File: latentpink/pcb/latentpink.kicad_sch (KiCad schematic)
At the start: 32 parts, among them M10 WEEE, M3 SCREWHOLE, M4 SCREWHOLE, M5 SCREWHOLE, M6 SCREWHOLE, M7 LONGTHING, M8 OSHW, M9 POLARITY, U36 AT30TS74_UDFN, U37 AT30TS74_UDFN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

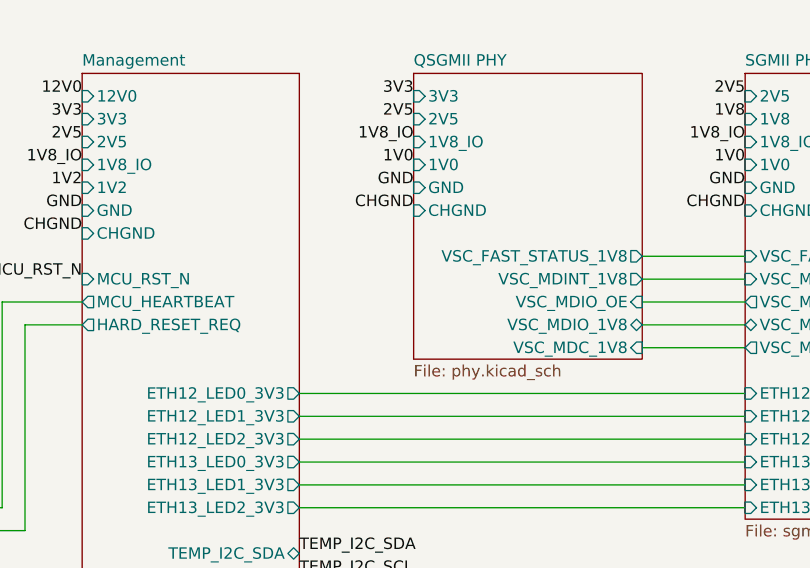
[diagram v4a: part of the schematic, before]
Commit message: Updated PCB layout with changes made during initial FPGA RTL dev
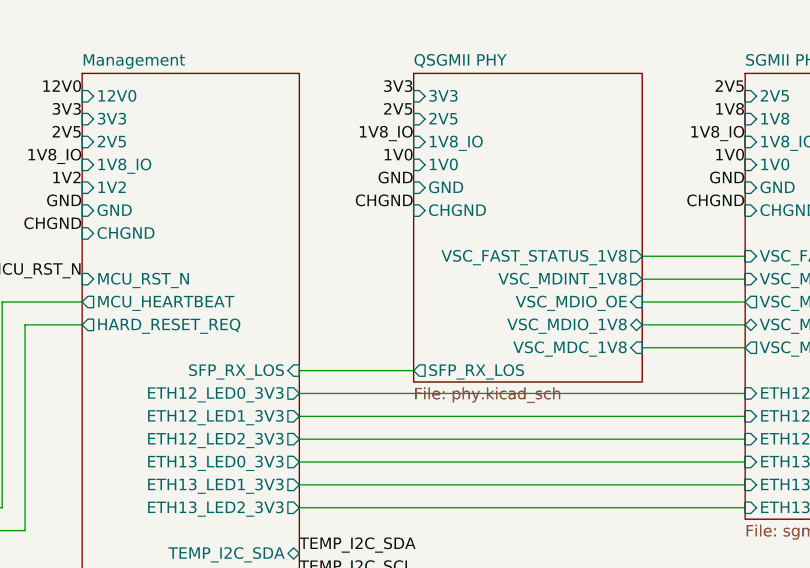
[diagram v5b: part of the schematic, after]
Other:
- sheet Management ports: added SFP_RX_LOS; removed none
- sheet QSGMII PHY ports: added SFP_RX_LOS; removed none
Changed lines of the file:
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@@
   (title_block
     (title "LATENTPINK - Top Level")
-    (date "2023-06-09")
+    (date "2023-06-15")
     (rev "0.1")
     (company "Antikernel Labs")
@@
   )
   (wire (pts (xy 190.5 43.18) (xy 201.93 43.18))
+    (stroke (width 0) (type default) (color 0 0 0 0))
+  )
+  (wire (pts (xy 152.4 55.88) (xy 165.1 55.88))
     (stroke (width 0) (type default) (color 0 0 0 0))
   )
@@
       (effects (font (size 1.27 1.27)) (justify right))
     )
+    (pin "SFP_RX_LOS" input (at 152.4 55.88 0)
+      (effects (font (size 1.27 1.27)) (justify right))
+    )
   )
   (sheet (at 201.93 22.86) (size 22.86 49.53) (fields_autoplaced)
@@
     )
   )
-  (sheet (at 165.1 22.86) (size 25.4 31.75) (fields_autoplaced)
+  (sheet (at 165.1 22.86) (size 25.4 34.29) (fields_autoplaced)
     (stroke (width 0.1524) (type solid) (color 0 0 0 0))
     (fill (color 0 0 0 0.0000))
@@
       (effects (font (size 1.27 1.27)) (justify left bottom))
     )
-    (property "Sheet file" "phy.kicad_sch" (id 1) (at 165.1 55.1946 0)
+    (property "Sheet file" "phy.kicad_sch" (id 1) (at 165.1 57.7346 0)
       (effects (font (size 1.27 1.27)) (justify left top))
     )
@@
     )
     (pin "1V8_IO" input (at 165.1 30.48 180)
+      (effects (font (size 1.27 1.27)) (justify left))
+    )
+    (pin "SFP_RX_LOS" output (at 165.1 55.88 180)
       (effects (font (size 1.27 1.27)) (justify left))
     )
@@
       (reference "C187") (unit 1) (value "0.47 uF") (footprint "azonenberg_pcb:EIA_0402_CAP_NOSILK")
     )
+    (path "/6c4b0638-d970-4292-bc58-db2e1b793524/d5990d76-6ad3-4bfd-a9be-5da547fd1224/96c4edd4-ce50-4a09-a53b-87b5a1a0fc47"
+      (reference "C188") (unit 1) (value "0.47 uF") (footprint "azonenberg_pcb:EIA_0402_CAP_NOSILK")
+    )
     (path "/6c4b0638-d970-4292-bc58-db2e1b793524/d5990d76-6ad3-4bfd-a9be-5da547fd1224/942373ed-08bf-4922-8211-11f3040b6b20"
       (reference "C189") (unit 1) (value "0.47 uF") (footprint "azonenberg_pcb:EIA_0402_CAP_NOSILK")
     )
+    (path "/6c4b0638-d970-4292-bc58-db2e1b793524/d5990d76-6ad3-4bfd-a9be-5da547fd1224/03eef2ac-07fc-4d6a-bbce-01046e92cb60"
+      (reference "C190") (unit 1) (value "0.47 uF") (footprint "azonenberg_pcb:EIA_0402_CAP_NOSILK")
+    )
     (path "/6c4b0638-d970-4292-bc58-db2e1b793524/d5990d76-6ad3-4bfd-a9be-5da547fd1224/da335c01-5e59-445c-8ce9-3cff99fa0a53"
       (reference "C191") (unit 1) (value "0.47 uF") (footprint "azonenberg_pcb:EIA_0402_CAP_NOSILK")
@@
       (reference "C448") (unit 1) (value "0.47 uF") (footprint "azonenberg_pcb:EIA_0402_CAP_NOSILK")
     )
+    (path "/6c4b0638-d970-4292-bc58-db2e1b793524/d5990d76-6ad3-4bfd-a9be-5da547fd1224/b9219748-1c2b-40c0-a041-7b1828d1e843"
+      (reference "C449") (unit 1) (value "0.47 uF") (footprint "azonenberg_pcb:EIA_0402_CAP_NOSILK")
+    )
     (path "/22109ef7-0bd2-46c3-8dd9-ecb52bedcbfa/94c46c58-24dc-4845-8aaa-ab3c82e370b2"
       (reference "C450") (unit 1) (value "0.1 uF") (footprint "azonenberg_pcb:EIA_0402_CAP_NOSILK")
@@
       (reference "C486") (unit 1) (value "0.47 uF") (footprint "azonenberg_pcb:EIA_0402_CAP_NOSILK")
     )
+    (path "/6c4b0638-d970-4292-bc58-db2e1b793524/d5990d76-6ad3-4bfd-a9be-5da547fd1224/2d28898f-1835-45c3-bf18-433bfa276226"
+      (reference "C487") (unit 1) (value "0.47 uF") (footprint "azonenberg_pcb:EIA_0402_CAP_NOSILK")
+    )
     (path "/70fb61fd-2f76-4850-9d6b-7e1d9a86570a/dacf15d0-cabc-4cac-8b1d-8797d78eacd5"

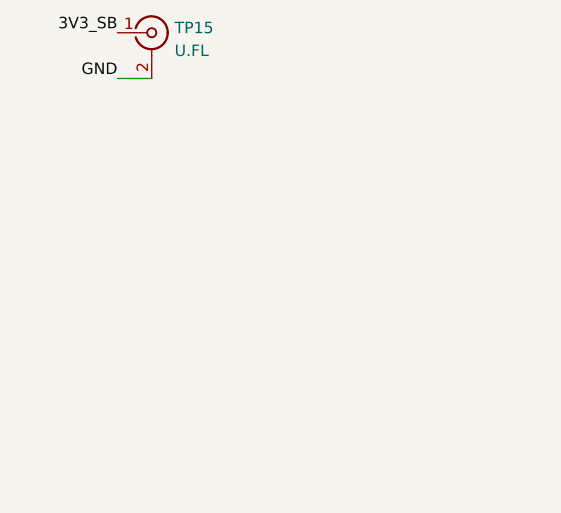
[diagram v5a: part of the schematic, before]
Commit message: Updated PCB during layout review with a bunch of fixes to MDI trace widths
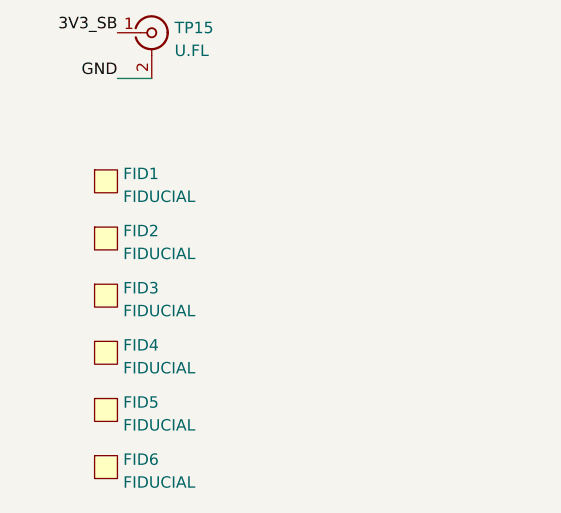
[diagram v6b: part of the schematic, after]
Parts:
- added FID1, FID2, FID3, FID4, FID5, FID6: FIDUCIAL, azonenberg_pcb:FIDUCIAL_1MM, symbol special-azonenberg:MECHANICAL
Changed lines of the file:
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@@
   (title_block
     (title "LATENTPINK - Top Level")
-    (date "2023-06-15")
+    (date "2023-06-24")
     (rev "0.1")
     (company "Antikernel Labs")
@@
     (pin "2")
   )
+  (symbol (lib_id "special-azonenberg:MECHANICAL") (at 27.94 243.84 0) (unit 1)
+    (in_bom yes) (on_board yes) (fields_autoplaced)
+    (property "Reference" "FID6" (id 0) (at 31.115 243.0053 0)
+      (effects (font (size 1.27 1.27)) (justify left))
+    )
+    (property "Value" "FIDUCIAL" (id 1) (at 31.115 245.5422 0)
+      (effects (font (size 1.27 1.27)) (justify left))
+    )
+    (property "Footprint" "azonenberg_pcb:FIDUCIAL_1MM" (id 2) (at 27.94 243.84 0)
+      (effects (font (size 1.27 1.27)) hide)
+    )
+    (property "Datasheet" "" (id 3) (at 27.94 243.84 0)
+      (effects (font (size 1.27 1.27)) hide)
+    )
+  )
   (symbol (lib_id "special-azonenberg:AT30TS74_UDFN") (at 298.45 54.61 0) (unit 1)
     (in_bom yes) (on_board yes) (fields_autoplaced)
@@
     )
   )
+  (symbol (lib_id "special-azonenberg:MECHANICAL") (at 27.94 212.09 0) (unit 1)
+    (in_bom yes) (on_board yes) (fields_autoplaced)
+    (property "Reference" "FID1" (id 0) (at 31.115 211.2553 0)
+      (effects (font (size 1.27 1.27)) (justify left))
+    )
+    (property "Value" "FIDUCIAL" (id 1) (at 31.115 213.7922 0)
+      (effects (font (size 1.27 1.27)) (justify left))
+    )
+    (property "Footprint" "azonenberg_pcb:FIDUCIAL_1MM" (id 2) (at 27.94 212.09 0)
+      (effects (font (size 1.27 1.27)) hide)
+    )
+    (property "Datasheet" "" (id 3) (at 27.94 212.09 0)
+      (effects (font (size 1.27 1.27)) hide)
+    )
+  )
   (symbol (lib_id "conn:CONN_01X01") (at 77.47 168.91 0) (unit 1)
     (in_bom yes) (on_board yes) (fields_autoplaced)
@@
     (pin "2")
   )
+  (symbol (lib_id "special-azonenberg:MECHANICAL") (at 27.94 231.14 0) (unit 1)
+    (in_bom yes) (on_board yes) (fields_autoplaced)
+    (property "Reference" "FID4" (id 0) (at 31.115 230.3053 0)
+      (effects (font (size 1.27 1.27)) (justify left))
+    )
+    (property "Value" "FIDUCIAL" (id 1) (at 31.115 232.8422 0)
+      (effects (font (size 1.27 1.27)) (justify left))
+    )
+    (property "Footprint" "azonenberg_pcb:FIDUCIAL_1MM" (id 2) (at 27.94 231.14 0)
+      (effects (font (size 1.27 1.27)) hide)
+    )
+    (property "Datasheet" "" (id 3) (at 27.94 231.14 0)
+      (effects (font (size 1.27 1.27)) hide)
+    )
+  )
   (symbol (lib_id "device:R") (at 73.66 118.11 90) (unit 1)
     (in_bom yes) (on_board yes) (fields_autoplaced)
@@
     (pin "2")
   )
+  (symbol (lib_id "special-azonenberg:MECHANICAL") (at 27.94 224.79 0) (unit 1)
+    (in_bom yes) (on_board yes) (fields_autoplaced)
+    (property "Reference" "FID3" (id 0) (at 31.115 223.9553 0)
+      (effects (font (size 1.27 1.27)) (justify left))
+    )
+    (property "Value" "FIDUCIAL" (id 1) (at 31.115 226.4922 0)
+      (effects (font (size 1.27 1.27)) (justify left))
+    )
+    (property "Footprint" "azonenberg_pcb:FIDUCIAL_1MM" (id 2) (at 27.94 224.79 0)
+      (effects (font (size 1.27 1.27)) hide)
+    )
+    (property "Datasheet" "" (id 3) (at 27.94 224.79 0)
+      (effects (font (size 1.27 1.27)) hide)
+    )
+  )
   (symbol (lib_id "conn:CONN_01X01") (at 370.84 237.49 0) (unit 1)
     (in_bom yes) (on_board yes) (fields_autoplaced)
@@
     (pin "1")
   )
+  (symbol (lib_id "special-azonenberg:MECHANICAL") (at 27.94 218.44 0) (unit 1)
+    (in_bom yes) (on_board yes) (fields_autoplaced)
+    (property "Reference" "FID2" (id 0) (at 31.115 217.6053 0)
+      (effects (font (size 1.27 1.27)) (justify left))
+    )
+    (property "Value" "FIDUCIAL" (id 1) (at 31.115 220.1422 0)
+      (effects (font (size 1.27 1.27)) (justify left))
+    )
+    (property "Footprint" "azonenberg_pcb:FIDUCIAL_1MM" (id 2) (at 27.94 218.44 0)
+      (effects (font (size 1.27 1.27)) hide)
+    )
+    (property "Datasheet" "" (id 3) (at 27.94 218.44 0)
+      (effects (font (size 1.27 1.27)) hide)
+    )
+  )
   (symbol (lib_id "conn:CONN_COAXIAL") (at 34.29 146.05 0) (unit 1)
     (in_bom yes) (on_board yes) (fields_autoplaced)
@@
     (pin "1")
     (pin "2")
+  )
+  (symbol (lib_id "special-azonenberg:MECHANICAL") (at 27.94 237.49 0) (unit 1)
+    (in_bom yes) (on_board yes) (fields_autoplaced)
+    (property "Reference" "FID5" (id 0) (at 31.115 236.6553 0)
+      (effects (font (size 1.27 1.27)) (justify left))
+    )
+    (property "Value" "FIDUCIAL" (id 1) (at 31.115 239.1922 0)
+      (effects (font (size 1.27 1.27)) (justify left))
+    )
+    (property "Footprint" "azonenberg_pcb:FIDUCIAL_1MM" (id 2) (at 27.94 237.49 0)
+      (effects (font (size 1.27 1.27)) hide)
+    )
+    (property "Datasheet" "" (id 3) (at 27.94 237.49 0)
+      (effects (font (size 1.27 1.27)) hide)
+    )
   )
   (symbol (lib_id "conn:CONN_01X01") (at 370.84 224.79 0) (unit 1)
@@
       (reference "FB11") (unit 1) (value "CIS21J121NE") (footprint "azonenberg_pcb:EIA_0805_INDUCTOR_NOSILK")
     )
+    (path "/62a1b210-35f7-4f57-b6dd-78b6c3b7f145"
+      (reference "FID1") (unit 1) (value "FIDUCIAL") (footprint "azonenberg_pcb:FIDUCIAL_1MM")
+    )
+    (path "/c9a405e7-c308-4d0e-9cc8-8f11bf837f05"
+      (reference "FID2") (unit 1) (value "FIDUCIAL") (footprint "azonenberg_pcb:FIDUCIAL_1MM")
+    )
+    (path "/a9374d82-4d05-40c0-b1fb-7726477e93ca"
+      (reference "FID3") (unit 1) (value "FIDUCIAL") (footprint "azonenberg_pcb:FIDUCIAL_1MM")
+    )
+    (path "/a3b0c695-fa88-423d-a88d-4dc5b8079de5"
+      (reference "FID4") (unit 1) (value "FIDUCIAL") (footprint "azonenberg_pcb:FIDUCIAL_1MM")
+    )
+    (path "/e0b2f428-9a95-430f-8ae9-b59e9df571a8"
+      (reference "FID5") (unit 1) (value "FIDUCIAL") (footprint "azonenberg_pcb:FIDUCIAL_1MM")
+    )
+    (path "/3fc1a4af-b0bf-4efd-96c8-6b7ea13a47d8"
+      (reference "FID6") (unit 1) (value "FIDUCIAL") (footprint "azonenberg_pcb:FIDUCIAL_1MM")
+    )
     (path "/d0e7363b-23d9-4272-a4d1-0db2834b87f3/4b168103-bbc3-44f6-be18-51ccfcb18e25"

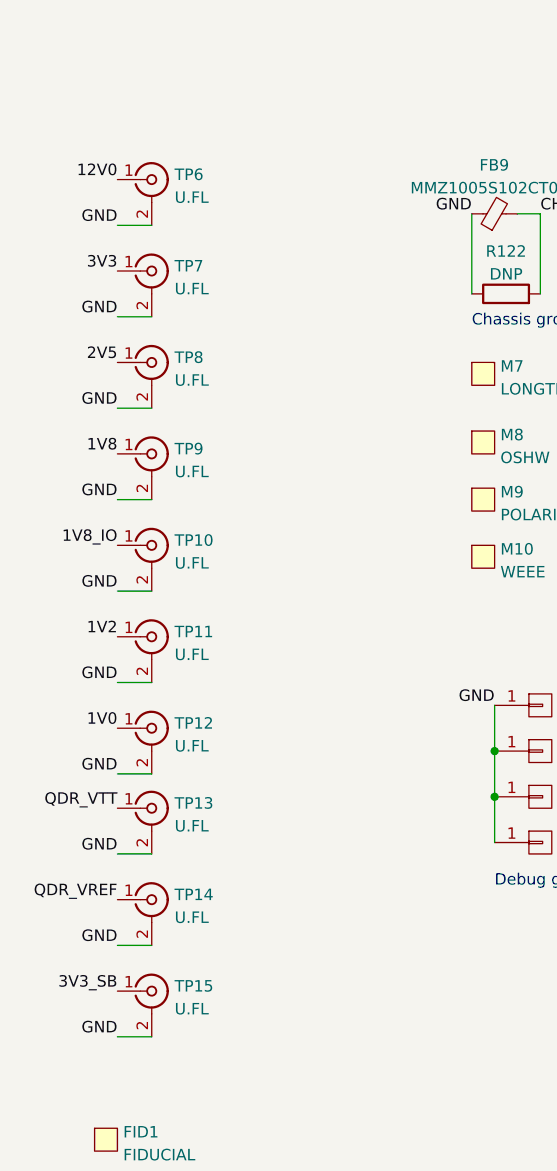
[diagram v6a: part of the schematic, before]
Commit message: Updated schematic with notes on power rail sequencing bug found during bringup
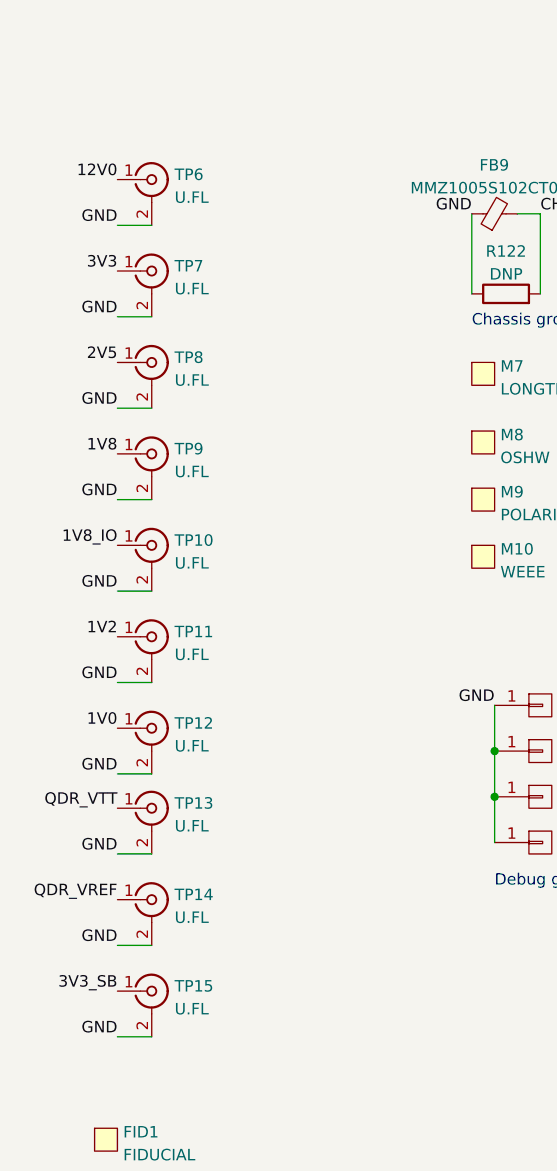
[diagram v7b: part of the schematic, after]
